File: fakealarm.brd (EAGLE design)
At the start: 28.1 x 34.5 mm, 17 parts, among them IC1 NE555N, Q1 2N3904, X1 RUN, X2 BAT, X3 GND, X4 +, X5 LED

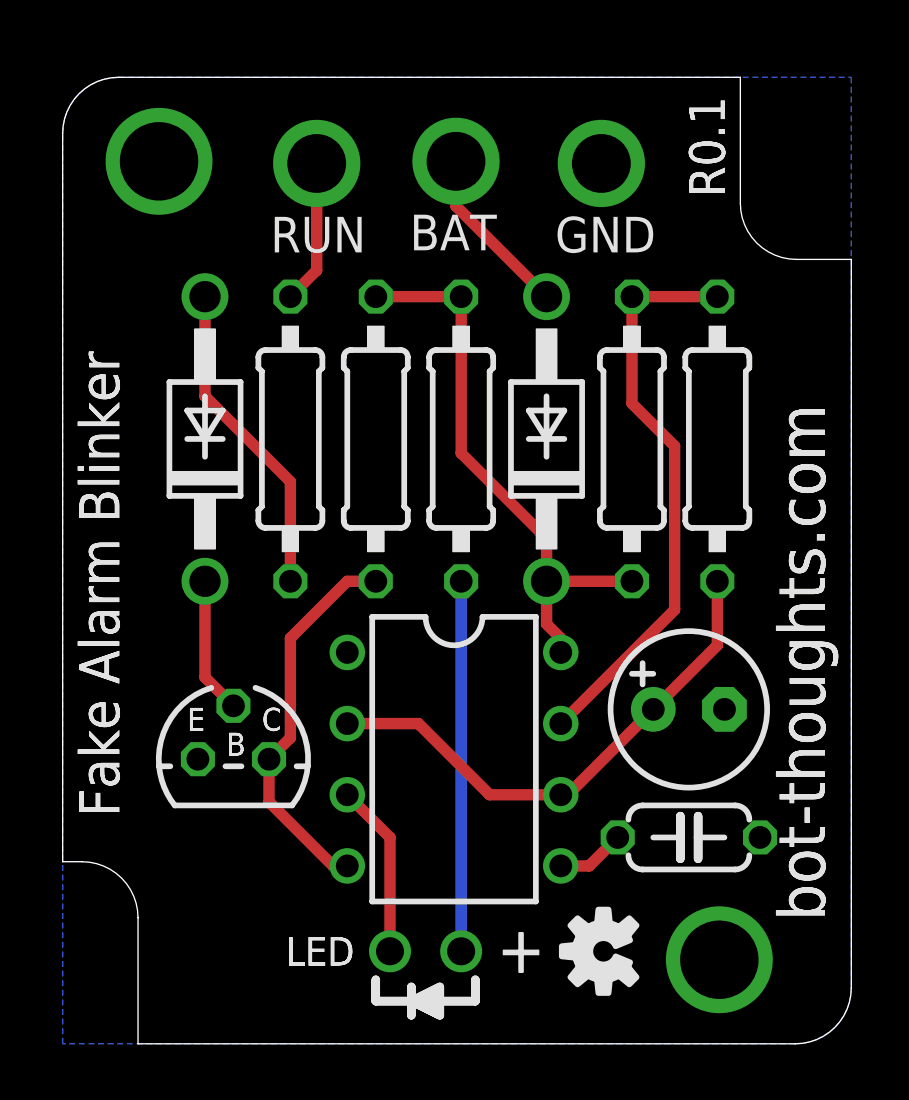
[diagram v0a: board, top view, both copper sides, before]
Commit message: redesigned for hammond 1551P (taller enclosure), respec'ed 33uF cap height and voltage, added documentation for max board height' '
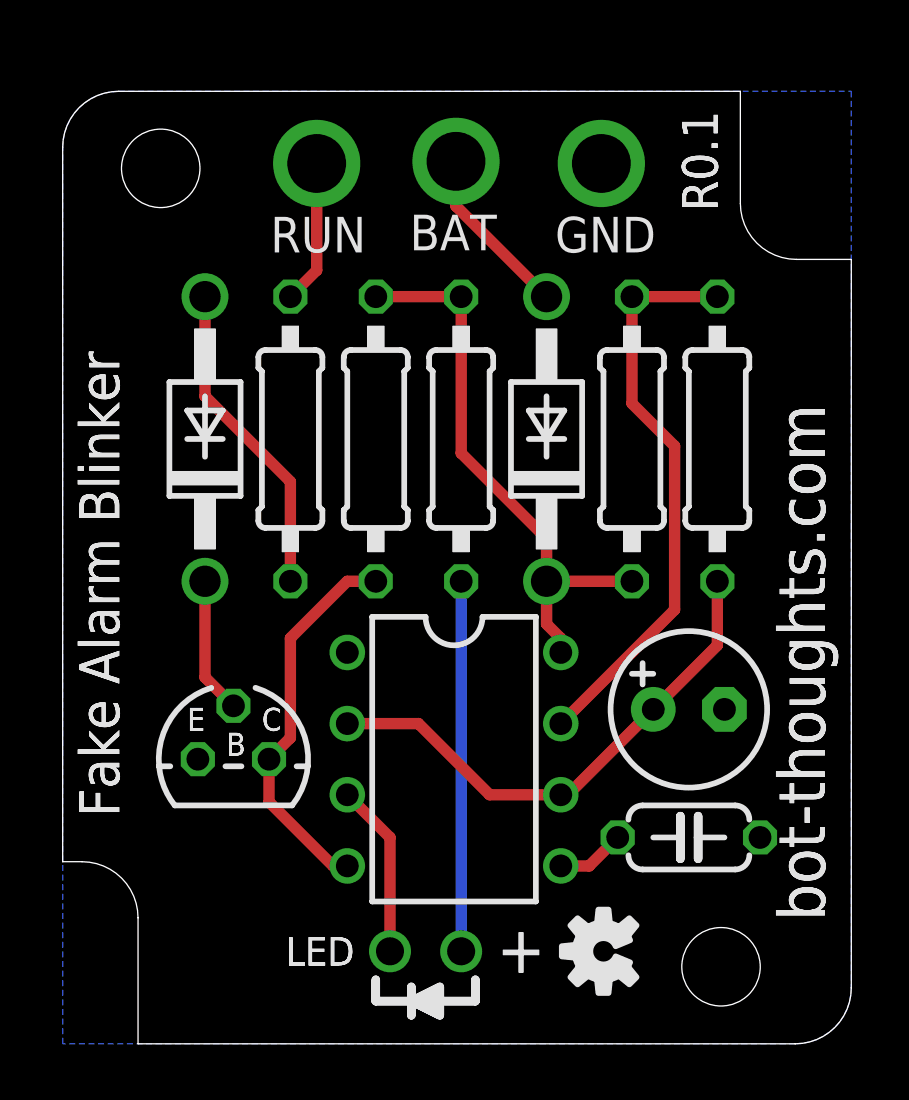
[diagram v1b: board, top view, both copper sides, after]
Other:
- board size 28.1 x 34.5 mm -> 28.1 x 34 mm
- board text added: "1.6mm PCB thickness"
- board text added: "10.4mm component height, max"
- board text added: "16.0mm inner height"
- board text added: "4.0mm PCB boss"
- board text added: "For Hammond 1551P"
- board text added: "Height"
- board text removed: "For Hammond 1551Q"
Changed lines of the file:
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@@
 <layer number="19" name="Unrouted" color="6" fill="1" visible="yes" active="yes"/>
 <layer number="20" name="Dimension" color="15" fill="1" visible="yes" active="yes"/>
-<layer number="21" name="tPlace" color="7" fill="1" visible="no" active="yes"/>
-<layer number="22" name="bPlace" color="7" fill="1" visible="no" active="yes"/>
-<layer number="23" name="tOrigins" color="15" fill="1" visible="no" active="yes"/>
-<layer number="24" name="bOrigins" color="15" fill="1" visible="no" active="yes"/>
-<layer number="25" name="tNames" color="7" fill="1" visible="no" active="yes"/>
-<layer number="26" name="bNames" color="7" fill="1" visible="no" active="yes"/>
-<layer number="27" name="tValues" color="7" fill="1" visible="no" active="yes"/>
-<layer number="28" name="bValues" color="7" fill="1" visible="no" active="yes"/>
+<layer number="21" name="tPlace" color="7" fill="1" visible="yes" active="yes"/>
+<layer number="22" name="bPlace" color="7" fill="1" visible="yes" active="yes"/>
+<layer number="23" name="tOrigins" color="15" fill="1" visible="yes" active="yes"/>
+<layer number="24" name="bOrigins" color="15" fill="1" visible="yes" active="yes"/>
+<layer number="25" name="tNames" color="7" fill="1" visible="yes" active="yes"/>
+<layer number="26" name="bNames" color="7" fill="1" visible="yes" active="yes"/>
+<layer number="27" name="tValues" color="7" fill="1" visible="yes" active="yes"/>
+<layer number="28" name="bValues" color="7" fill="1" visible="yes" active="yes"/>
 <layer number="29" name="tStop" color="7" fill="3" visible="yes" active="yes"/>
 <layer number="30" name="bStop" color="7" fill="6" visible="yes" active="yes"/>
@@
 <layer number="43" name="vRestrict" color="2" fill="10" visible="no" active="yes"/>
 <layer number="44" name="Drills" color="7" fill="1" visible="no" active="yes"/>
-<layer number="45" name="Holes" color="7" fill="1" visible="no" active="yes"/>
+<layer number="45" name="Holes" color="7" fill="1" visible="yes" active="yes"/>
 <layer number="46" name="Milling" color="3" fill="1" visible="no" active="yes"/>
 <layer number="47" name="Measures" color="7" fill="1" visible="no" active="yes"/>
@@
 <wire x1="26.15" y1="0" x2="28.15" y2="2" width="0" layer="20" curve="90"/>
 <wire x1="28.15" y1="2" x2="28.15" y2="28" width="0" layer="20"/>
-<wire x1="24.19" y1="34.5" x2="2" y2="34.5" width="0" layer="20"/>
-<wire x1="2" y1="34.5" x2="0" y2="32.5" width="0" layer="20" curve="90"/>
-<wire x1="0" y1="32.5" x2="0" y2="6.5" width="0" layer="20"/>
+<wire x1="24.19" y1="34" x2="2" y2="34" width="0" layer="20"/>
+<wire x1="2" y1="34" x2="0" y2="32" width="0" layer="20" curve="90"/>
+<wire x1="0" y1="32" x2="0" y2="6.5" width="0" layer="20"/>
 <text x="2.02" y="8.102" size="1.4224" layer="25" font="vector" ratio="12" rot="R90">Fake Alarm Blinker</text>
 <text x="27.208" y="4.396" size="1.6764" layer="25" font="vector" ratio="12" rot="R90">bot-thoughts.com</text>
-<text x="23.636" y="30.23" size="1.27" layer="25" font="vector" ratio="12" rot="R90">R0.1</text>
-<text x="4.054" y="35.6" size="1.27" layer="48" font="vector" ratio="12">For Hammond 1551Q</text>
-<wire x1="24.19" y1="34.5" x2="24.19" y2="30" width="0" layer="20"/>
+<text x="23.382" y="29.722" size="1.27" layer="25" font="vector" ratio="12" rot="R90">R0.1</text>
+<text x="1.006" y="47.03" size="1.27" layer="48" font="vector" ratio="12">For Hammond 1551P</text>
+<wire x1="24.19" y1="34" x2="24.19" y2="30" width="0" layer="20"/>
 <wire x1="24.19" y1="30" x2="26.19" y2="28" width="0" layer="20" curve="90"/>
 <wire x1="26.19" y1="28" x2="28.15" y2="28" width="0" layer="20"/>
@@
 <text x="2.0200125" y="8.101990625" size="1.4224" layer="121" font="vector" ratio="15" rot="R90">Fake Alarm Blinker</text>
 <text x="27.207996875" y="4.396003125" size="1.6764" layer="121" font="vector" ratio="13" rot="R90">bot-thoughts.com</text>
-<text x="23.635996875" y="30.2299875" size="1.27" layer="121" font="vector" ratio="16" rot="R90">R0.1</text>
+<text x="23.381996875" y="29.7219875" size="1.27" layer="121" font="vector" ratio="16" rot="R90">R0.1</text>
 <text x="7.417003125" y="28.248990625" size="1.27" layer="121" font="vector" ratio="16">RUN</text>
 <text x="12.389003125" y="28.3249875" size="1.27" layer="121" font="vector" ratio="16">BAT</text>
@@
 <text x="10.6426" y="19.9644" size="0.9906" layer="122" font="vector" ratio="21" rot="MR90">100K</text>
 <text x="13.6906" y="20.9804" size="0.9906" layer="122" font="vector" ratio="21" rot="MR90">1K</text>
+<hole x="3.5" y="31.25" drill="2.8"/>
+<hole x="23.5" y="2.75" drill="2.8"/>
+<text x="3.048" y="42.418" size="1.27" layer="48" font="vector" ratio="10">16.0mm inner height</text>
+<text x="4.318" y="40.386" size="1.27" layer="48" font="vector" ratio="10">4.0mm PCB boss</text>
+<text x="4.318" y="38.354" size="1.27" layer="48" font="vector" ratio="10">1.6mm PCB thickness</text>
+<text x="3.302" y="35.814" size="1.27" layer="48" font="vector" ratio="10">10.4mm component height, max</text>
+<text x="1.778" y="44.45" size="1.27" layer="48" font="vector" ratio="10">Height</text>
+<wire x1="1.778" y1="37.592" x2="9.652" y2="37.592" width="0.254" layer="48"/>
 </plain>
 <attributes>
@@
 <element name="C1" library="rcl" package="E2,5-6" value="33uF" x="22.352" y="11.938" smashed="yes">
 <attribute name="VALUE" x="20.447" y="10.414" size="1.016" layer="28" font="vector" ratio="10" rot="MR180"/>
-<attribute name="VOLTAGE" value="25V" x="22.352" y="11.938" size="1.778" layer="27" display="off"/>
+<attribute name="VOLTAGE" value="35V" x="22.352" y="11.938" size="1.778" layer="27" display="off"/>
+<attribute name="HEIGHT" value="10mm MAX" x="22.352" y="11.938" size="1.778" layer="27" display="off"/>
 </element>
 <element name="IC1" library="linear" package="DIL08" value="NE555N" x="13.97" y="10.16" smashed="yes" rot="R270">
@@
 <polygon width="0.4064" layer="16">
 <vertex x="0" y="0"/>
-<vertex x="0" y="32.5" curve="-90"/>
-<vertex x="2" y="34.5"/>
-<vertex x="28.15" y="34.5"/>
+<vertex x="0" y="32" curve="-90"/>
+<vertex x="2" y="34"/>
+<vertex x="28.15" y="34"/>
 <vertex x="28.15" y="2" curve="-90"/>
 <vertex x="26.15" y="0"/>
 </polygon>
-<via x="3.44" y="31.5" extent="1-16" drill="2.8"/>
-<via x="23.44" y="3" extent="1-16" drill="2.8"/>
 <contactref element="C1" pad="-"/>
 <contactref element="C2" pad="2"/>

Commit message: Revised switch to use two mosfets to switch entire 555, revised layout, silk, added enclosure info to board
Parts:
- removed D1, D2: 1N4004, diode:DO41-10
- added Q2: 2N7000, ads4:TO92D-
- IC1: value NE555N -> LTC555
- LOGO1: value OSHW-LOGOS -> OSHW-LOGOM; device SparkFun-Aesthetics:OSHW-LOGO-S -> SparkFun-Aesthetics:OSHW-LOGO-M
- Q1: value 2N3904 -> 2N7000; device bt_transistor:TO92 -> ads4:TO92D-
- R3: value 1K -> 10k
- R4: value 100K -> 10k
- moved Q1 16.0 mm to (12.3, 24.9), turned to 270 degrees
- moved LOGO1 13.6 mm to (5.71, 3.56)
- moved R3 8.51 mm to (16.6, 21.6)
- moved R5 8.25 mm to (5.97, 21.6)
- moved X2 5.66 mm to (8.38, 31.2)
- moved X1 4.40 mm to (13.5, 31.2)
- moved X4 3.18 mm to (11.0, 3.30), turned to 180 degrees
- moved R4 2.16 mm to (9.02, 21.6), turned to 90 degrees
- moved X5 1.91 mm to (13.6, 3.30), turned to 0 degrees
- moved X3 0.71 mm to (18.5, 31.2)
- moved C1 0.64 mm to (21.7, 11.9)
- moved C2 0.64 mm to (21.7, 7.37)
- moved R1 0.64 mm to (19.7, 21.6)
- moved IC1 0.63 mm to (13.3, 10.2)
- moved R2 0.63 mm to (22.7, 21.6)
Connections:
- removed net N$11: IC1.4, Q1.1, R4.2
- removed net N$6: D2.A, X2.P$1
- net 12V: now also IC1.4, X2.P$1; no longer D2.C
- net GND: now also Q1.1, Q2.1, R3.2; no longer IC1.1, Q1.3
- net N$1: now also Q1.3, Q2.2, R4.2; no longer D1.A, R3.1
- net N$2: now also R3.1, X1.P$1; no longer D1.C
- net N$5: now also IC1.1, Q2.3; no longer R3.2, X1.P$1
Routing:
- net 12V: track 20.3 -> 41.8 mm
- net N$11: track 13.8 -> 0.00 mm
- net N$2: track 4.87 -> 17.6 mm
- net N$6: track 6.17 -> 0.00 mm
- net N$9: track 13.2 -> 15.8 mm
- net N$1: track 11.4 -> 9.91 mm
- net N$10: track 6.22 -> 7.27 mm
- net N$5: track 5.14 -> 4.59 mm
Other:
- board size 28.1 x 34 mm -> 25.9 x 34 mm
- board text added: "R0.2"
- board text removed: "2N3904"
- board text removed: "B"
- board text removed: "C"
- board text removed: "E"

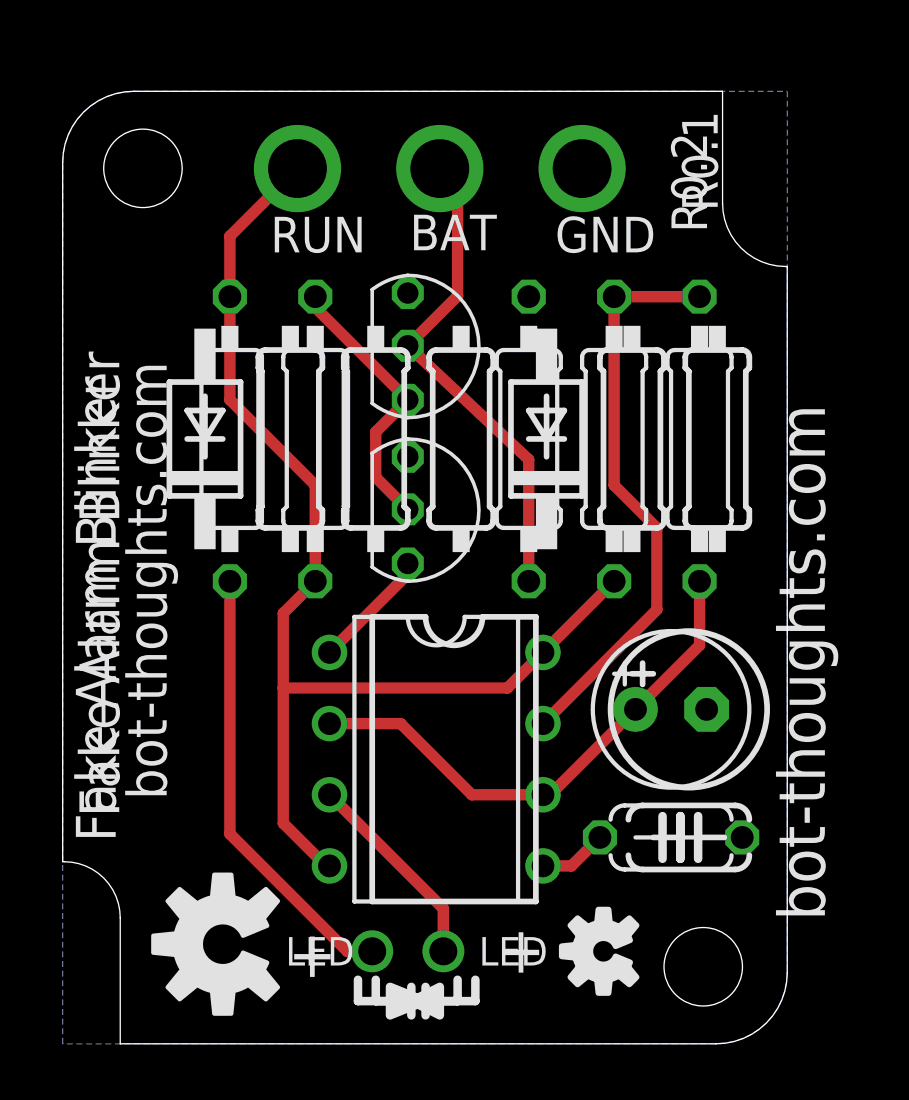
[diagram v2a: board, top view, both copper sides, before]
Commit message: Layout tweaks on board and schematic. Added reverse protection diode
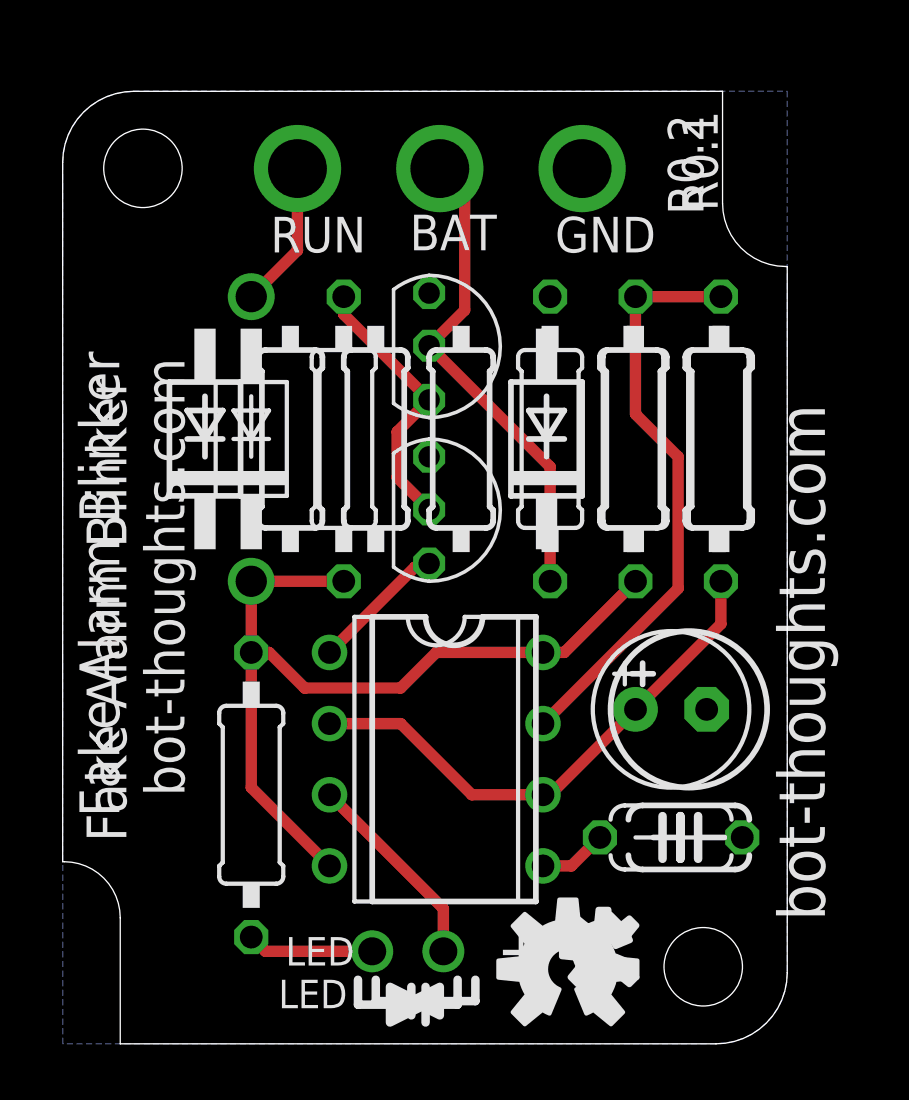
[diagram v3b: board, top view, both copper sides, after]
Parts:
- added D1: 1N4004, diode:DO41-10
- X4: value + -> LED
- X5: value LED -> LEDC
- moved R5 12.7 mm to (6.73, 8.89)
- moved LOGO1 12.4 mm to (18.0, 2.67), turned to 0 degrees
- moved R4 1.02 mm to (10.0, 21.6)
- moved R1 0.76 mm to (20.4, 21.6)
- moved R2 0.76 mm to (23.5, 21.6)
- moved R3 0.76 mm to (17.4, 21.6)
- moved Q1 0.76 mm to (13.1, 24.9)
- moved Q2 0.76 mm to (13.1, 19.1)
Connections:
- new net N$6: D1.A, X2.P$1
- net 12V: now also D1.C; no longer X2.P$1
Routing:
- net 12V: track 41.8 -> 30.4 mm
- net N$9: track 15.8 -> 4.53 mm
- net N$6: track 0.00 -> 5.26 mm
